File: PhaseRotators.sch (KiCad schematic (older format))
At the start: 10 parts, among them U1 74LVC1G74, U2 74LVC74APW, U3 74LVC74APW, U4 74LVC1G74

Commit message: first edit
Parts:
- removed U1, U4: 74LVC1G74, Housings_SSOP:TSSOP-8_3x3mm_Pitch0.65mm, symbol 74LVC1G74
- removed U3: 74LVC74APW, Housings_SSOP:TSSOP-14_4.4x5mm_Pitch0.65mm, symbol 74LS74
- added R8: 1k, Resistors_SMD:R_0603_HandSoldering, symbol R_Small
- C1, C2: footprint UI:C_1206_0603 -> Capacitors_SMD:C_0603_HandSoldering
- C3: footprint Capacitors_THT:CP_Radial_D5.0mm_P2.00mm -> Capacitors_Tantalum_SMD:CP_Tantalum_Case-A_EIA-3216-18_Wave
- L1: footprint Resistors_THT:R_Axial_DIN0207_L6.3mm_D2.5mm_P10.16mm_Horizontal -> Choke_Axial_ThroughHole:Choke_Horizontal_RM10mm
- R1, R2: footprint UI:R_1206_0603 -> Resistors_SMD:R_0603_HandSoldering
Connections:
- net RX0 is gone; now on an unnamed net: U2.11 (Cp)
- net RX180 is gone; now on an unnamed net: U2.3 (Cp)
- net CLK: now also R2.1
- net GND: now also R8.2
- net at U2.6 (~Q): now also U2.12 (D)
- net P0: now reaches U2.8 (~Q)
- net P0: no longer U2.12 (D)
- net at C1.1, R1.2: now also R8.1; no longer R2.1
- net RX_P0 renamed P90
- net RX_P90: no longer names the net of U2.2 (D), U2.9 (Q)
- net Voltage2 renamed Voltage1
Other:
- moved on the sheet: C1, C2, C3, L1, R1, U2A, U2B

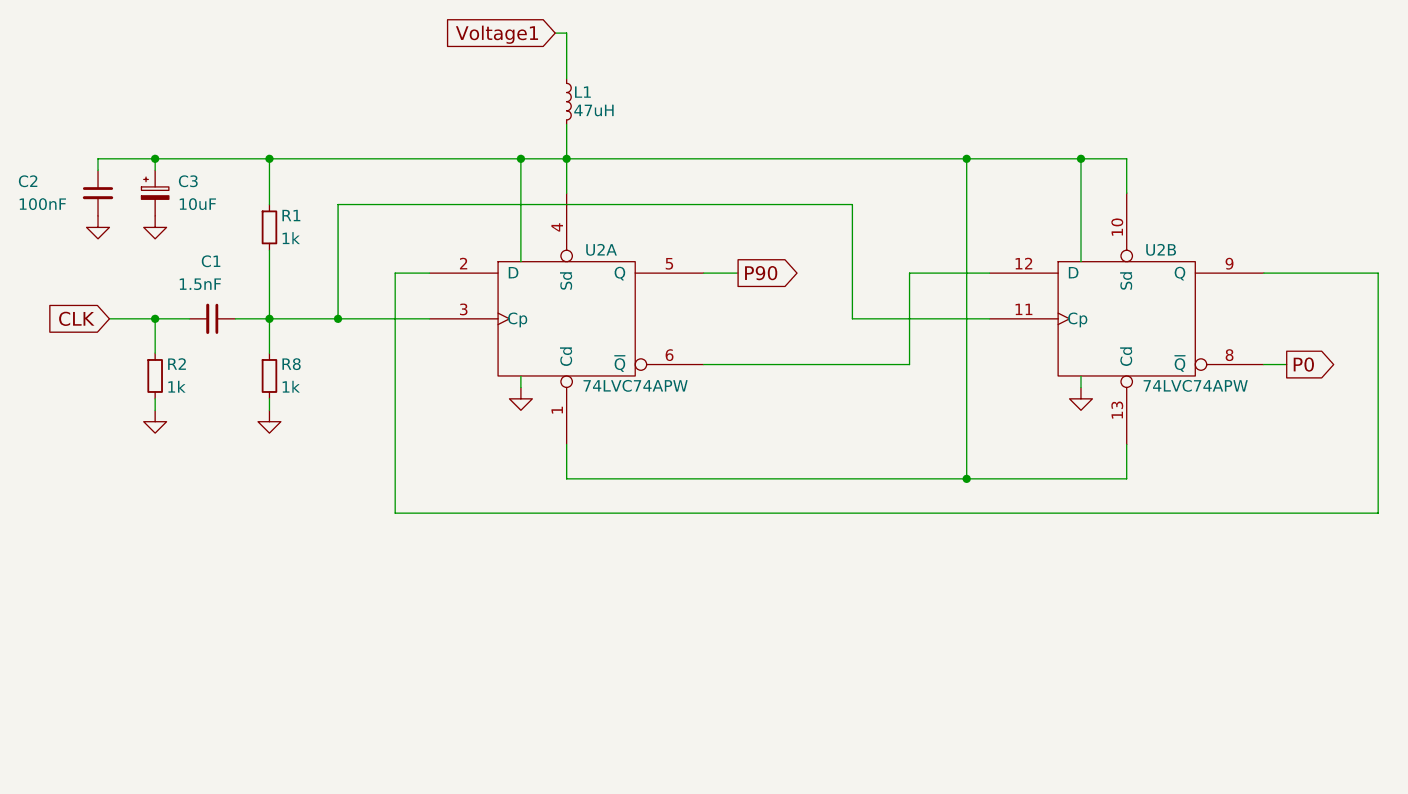
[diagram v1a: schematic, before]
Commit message: rotators 2 74lvc1G74
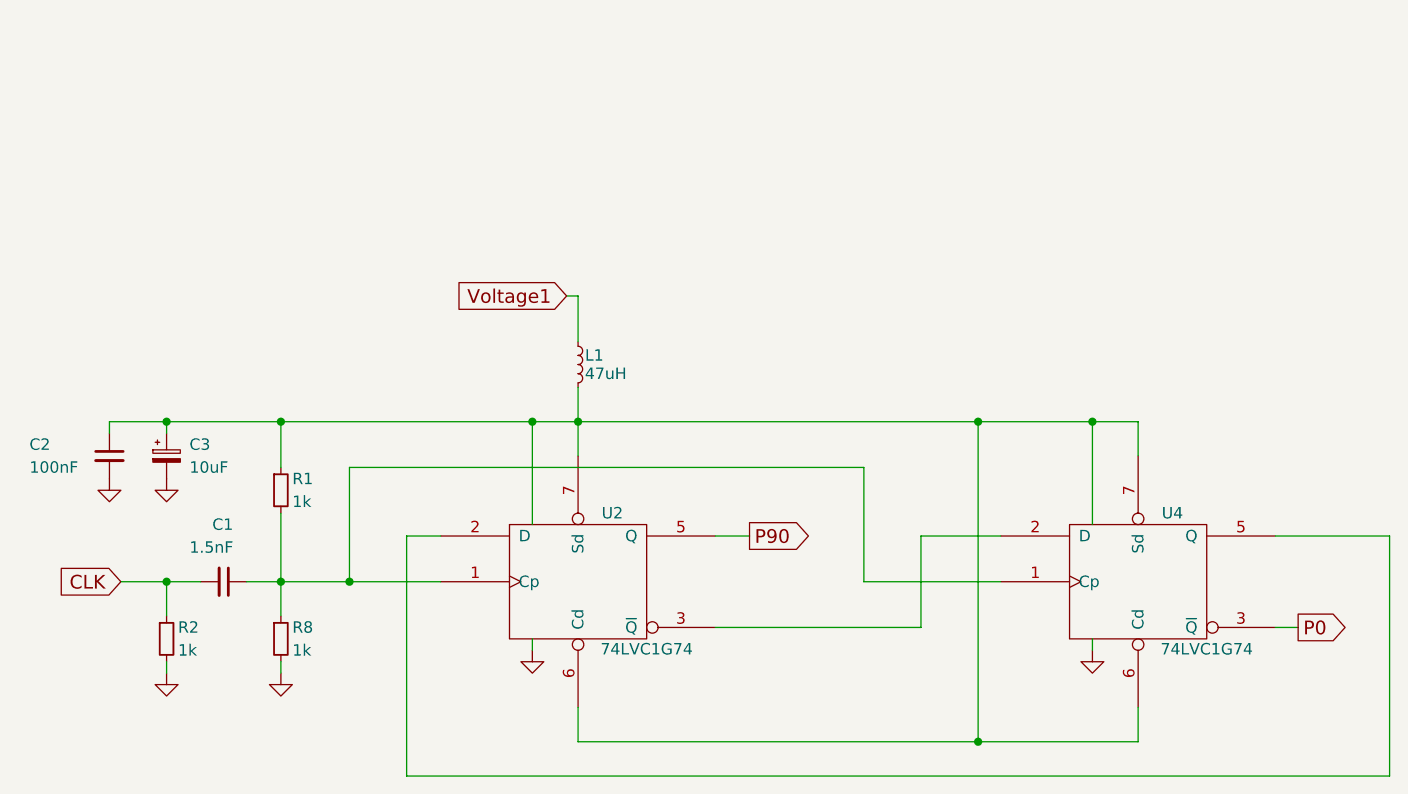
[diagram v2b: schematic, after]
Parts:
- removed U2: 74LVC74APW, Housings_SSOP:TSSOP-14_4.4x5mm_Pitch0.65mm, symbol 74LS74
- added U2, U4: 74LVC1G74, Housings_SSOP:TSSOP-8_4.4x3mm_Pitch0.65mm, symbol 74LVC1G74
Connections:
- net GND: now also U2.4 (GND), U4.4 (GND)
- net P0: now also U4.3 (~Q)
- net P90: now also U2.5 (Q)
- net VCC: now also U2.6 (Cd), U2.7 (Sd), U2.8 (VCC), U4.6 (Cd), U4.7 (Sd), U4.8 (VCC)
- net at C1.1, R1.2, R8.1: now also U2.1 (Cp), U4.1 (Cp)
- new net: U2.2 (D), U4.5 (Q)
- new net: U2.3 (~Q), U4.2 (D)
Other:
- moved on the sheet: C1, C2, C3, L1, R1, R2, R8

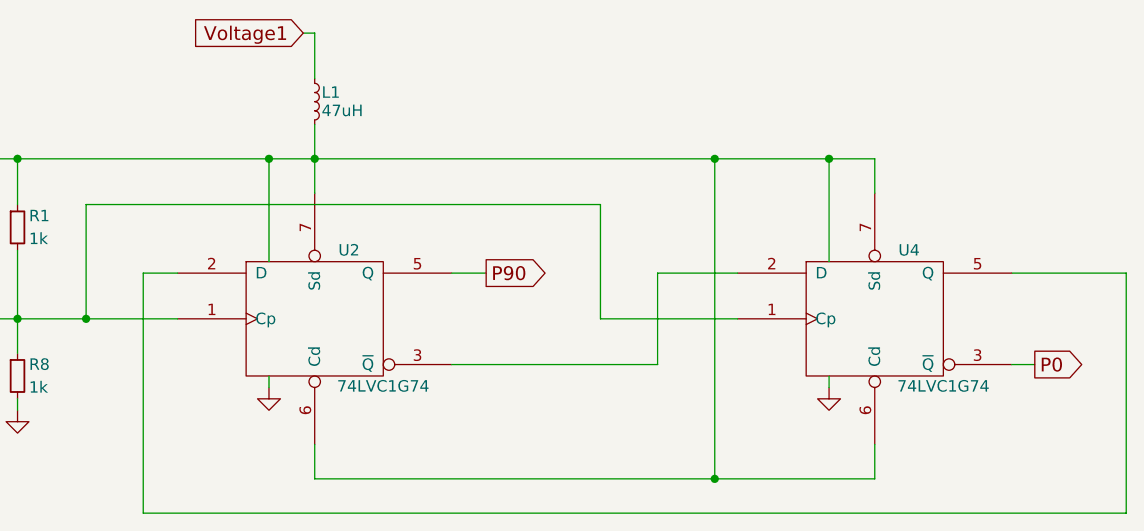
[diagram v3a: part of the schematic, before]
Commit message: need some GND vias
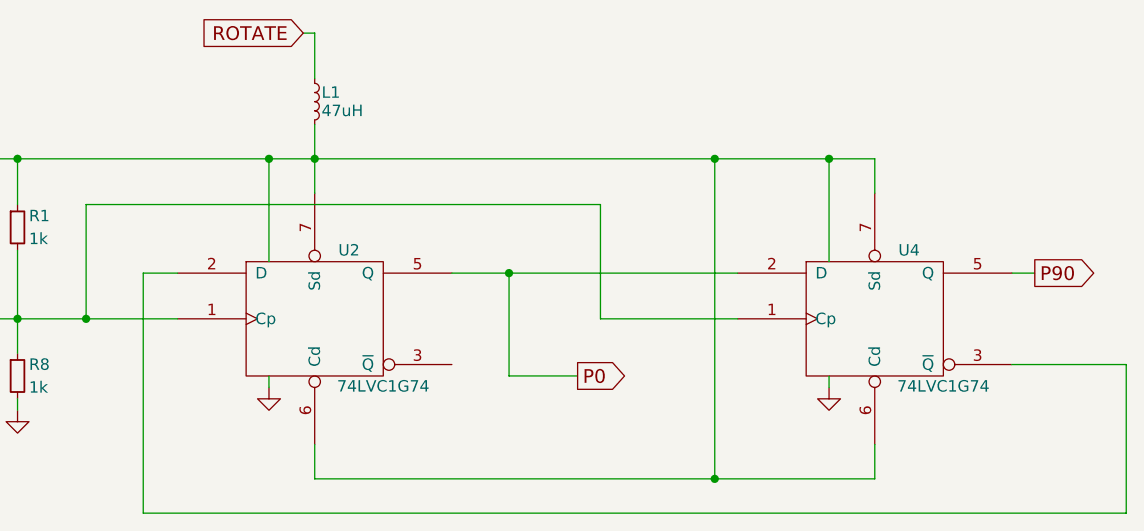
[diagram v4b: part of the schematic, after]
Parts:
- C1, C2: footprint Capacitors_SMD:C_0603_HandSoldering -> UI:C_1206_0603
- C3: footprint Capacitors_Tantalum_SMD:CP_Tantalum_Case-A_EIA-3216-18_Wave -> Capacitors_THT:CP_Radial_D5.0mm_P2.00mm
- R1, R2, R8: footprint Resistors_SMD:R_0603_HandSoldering -> UI:R_1206_0603
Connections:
- net P0: now also U2.5 (Q), U4.2 (D); no longer U4.3 (~Q)
- net P90: now also U4.5 (Q); no longer U2.5 (Q)
- net at U2.2 (D): now also U4.3 (~Q); no longer U4.5 (Q)
- net at U2.3 (~Q): no longer U4.2 (D)
- net Voltage1 renamed ROTATE
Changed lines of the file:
@@
 $Descr A4 11693 8268
 encoding utf-8
-Sheet 5 8
+Sheet 5 7
 Title ""
 Date ""
@@
 	4250 3250 4100 3250
 $Comp
-L GND #PWR019
+L GND #PWR040
 U 1 1 5EACACD6
 P 7100 3750
-F 0 "#PWR019" H 7100 3500 50  0001 C CNN
+F 0 "#PWR040" H 7100 3500 50  0001 C CNN
 F 1 "GND" H 7100 3600 50  0001 C CNN
 F 2 "" H 7100 3750 50  0001 C CNN
@@
 	7100 3750 7100 3700
 $Comp
-L GND #PWR020
+L GND #PWR041
 U 1 1 5EACAD11
 P 4650 3750
-F 0 "#PWR020" H 4650 3500 50  0001 C CNN
+F 0 "#PWR041" H 4650 3500 50  0001 C CNN
 F 1 "GND" H 4650 3600 50  0001 C CNN
 F 2 "" H 4650 3750 50  0001 C CNN
@@
 	4650 3750 4650 3700
 Wire Wire Line
-	6700 3250 6350 3250
+	5450 3250 6700 3250
 Wire Wire Line
 	3400 3450 4250 3450
@@
 Wire Wire Line
 	4100 4300 8400 4300
-Wire Wire Line
-	8400 4300 8400 3250
 $Comp
 L R_Small R1
@@
 F 0 "R1" H 3600 3100 50  0000 L CNN
 F 1 "1k" H 3600 3000 50  0000 L CNN
-F 2 "Resistors_SMD:R_0603_HandSoldering" H 3550 3050 50  0001 C CNN
+F 2 "UI:R_1206_0603" H 3550 3050 50  0001 C CNN
 F 3 "" H 3550 3050 50  0001 C CNN
 	1    3550 3050
@@
 F 0 "C1" V 3050 3400 50  0000 L CNN
 F 1 "1.5nF" V 3150 3300 50  0000 L CNN
-F 2 "Capacitors_SMD:C_0603_HandSoldering" H 3300 3450 50  0001 C CNN
+F 2 "UI:C_1206_0603" H 3300 3450 50  0001 C CNN
 F 3 "" H 3300 3450 50  0001 C CNN
 	1    3300 3450
@@
 F 0 "C3" H 3150 2950 50  0000 L CNN
 F 1 "10uF" H 3150 2850 50  0000 L CNN
-F 2 "Capacitors_Tantalum_SMD:CP_Tantalum_Case-A_EIA-3216-18_Wave" H 3050 2900 50  0001 C CNN
+F 2 "Capacitors_THT:CP_Radial_D5.0mm_P2.00mm" H 3050 2900 50  0001 C CNN
 F 3 "" H 3050 2900 50  0001 C CNN
 	1    3050 2900
@@
 Connection ~ 4650 2750
 $Comp
-L GND #PWR021
+L GND #PWR042
 U 1 1 5EAC7395
 P 3050 3000
-F 0 "#PWR021" H 3050 2750 50  0001 C CNN
+F 0 "#PWR042" H 3050 2750 50  0001 C CNN
 F 1 "GND" H 3050 2850 50  0001 C CNN
 F 2 "" H 3050 3000 50  0001 C CNN
@@
 F 0 "C2" H 2450 2950 50  0000 L CNN
 F 1 "100nF" H 2450 2850 50  0000 L CNN
-F 2 "Capacitors_SMD:C_0603_HandSoldering" H 2800 2900 50  0001 C CNN
+F 2 "UI:C_1206_0603" H 2800 2900 50  0001 C CNN
 F 3 "" H 2800 2900 50  0001 C CNN
 	1    2800 2900
@@
 $EndComp
 $Comp
-L GND #PWR022
+L GND #PWR043
 U 1 1 5EAC76D0
 P 2800 3000
-F 0 "#PWR022" H 2800 2750 50  0001 C CNN
+F 0 "#PWR043" H 2800 2750 50  0001 C CNN
 F 1 "GND" H 2800 2850 50  0001 C CNN
 F 2 "" H 2800 3000 50  0001 C CNN
@@
 	1    0    0    -1
 $EndComp
-Text GLabel 5600 3250 2    60   Output ~ 0
+Text GLabel 6000 3700 2    60   Output ~ 0
+P0
+Text GLabel 8000 3250 2    60   Output ~ 0
 P90
-Text GLabel 8000 3650 2    60   Output ~ 0
-P0
 Text GLabel 4800 2200 0    60   Input ~ 0
-Voltage1
+ROTATE
 Wire Wire Line
 	4800 2200 4850 2200
@@
 	6100 2950 3850 2950
 Connection ~ 3850 3450
-Wire Wire Line
-	6350 3250 6350 3650
-Wire Wire Line
-	6350 3650 5450 3650
-Wire Wire Line
-	8400 3250 7900 3250
-Wire Wire Line
-	5450 3250 5600 3250
-Wire Wire Line
-	7900 3650 8000 3650
 Wire Wire Line
 	3550 3150 3550 3600
@@
 F 0 "R8" H 3600 3750 50  0000 L CNN
 F 1 "1k" H 3600 3650 50  0000 L CNN
-F 2 "Resistors_SMD:R_0603_HandSoldering" H 3550 3700 50  0001 C CNN
+F 2 "UI:R_1206_0603" H 3550 3700 50  0001 C CNN
 F 3 "" H 3550 3700 50  0001 C CNN
 	1    3550 3700
@@
 	3850 2950 3850 3450
 $Comp
-L GND #PWR023
+L GND #PWR044
 U 1 1 5EB0156A
 P 3550 3850
-F 0 "#PWR023" H 3550 3600 50  0001 C CNN
+F 0 "#PWR044" H 3550 3600 50  0001 C CNN
 F 1 "GND" H 3550 3700 50  0001 C CNN
 F 2 "" H 3550 3850 50  0001 C CNN
@@
 F 0 "R2" H 3100 3750 50  0000 L CNN
 F 1 "1k" H 3100 3650 50  0000 L CNN
-F 2 "Resistors_SMD:R_0603_HandSoldering" H 3050 3700 50  0001 C CNN
+F 2 "UI:R_1206_0603" H 3050 3700 50  0001 C CNN
 F 3 "" H 3050 3700 50  0001 C CNN
 	1    3050 3700
@@
 $EndComp
 $Comp
-L GND #PWR024
+L GND #PWR045
 U 1 1 5EB016D4
 P 3050 3850
-F 0 "#PWR024" H 3050 3600 50  0001 C CNN
+F 0 "#PWR045" H 3050 3600 50  0001 C CNN
 F 1 "GND" H 3050 3700 50  0001 C CNN
 F 2 "" H 3050 3850 50  0001 C CNN
@@
 	1    0    0    -1
 $EndComp
+Wire Wire Line
+	8400 4300 8400 3650
+Wire Wire Line
+	5700 3250 5700 3700
+Connection ~ 5700 3250
+Wire Wire Line
+	7900 3250 8000 3250
+Wire Wire Line
+	8400 3650 7900 3650
+Wire Wire Line
+	5700 3700 6000 3700
 $EndSCHEMATC

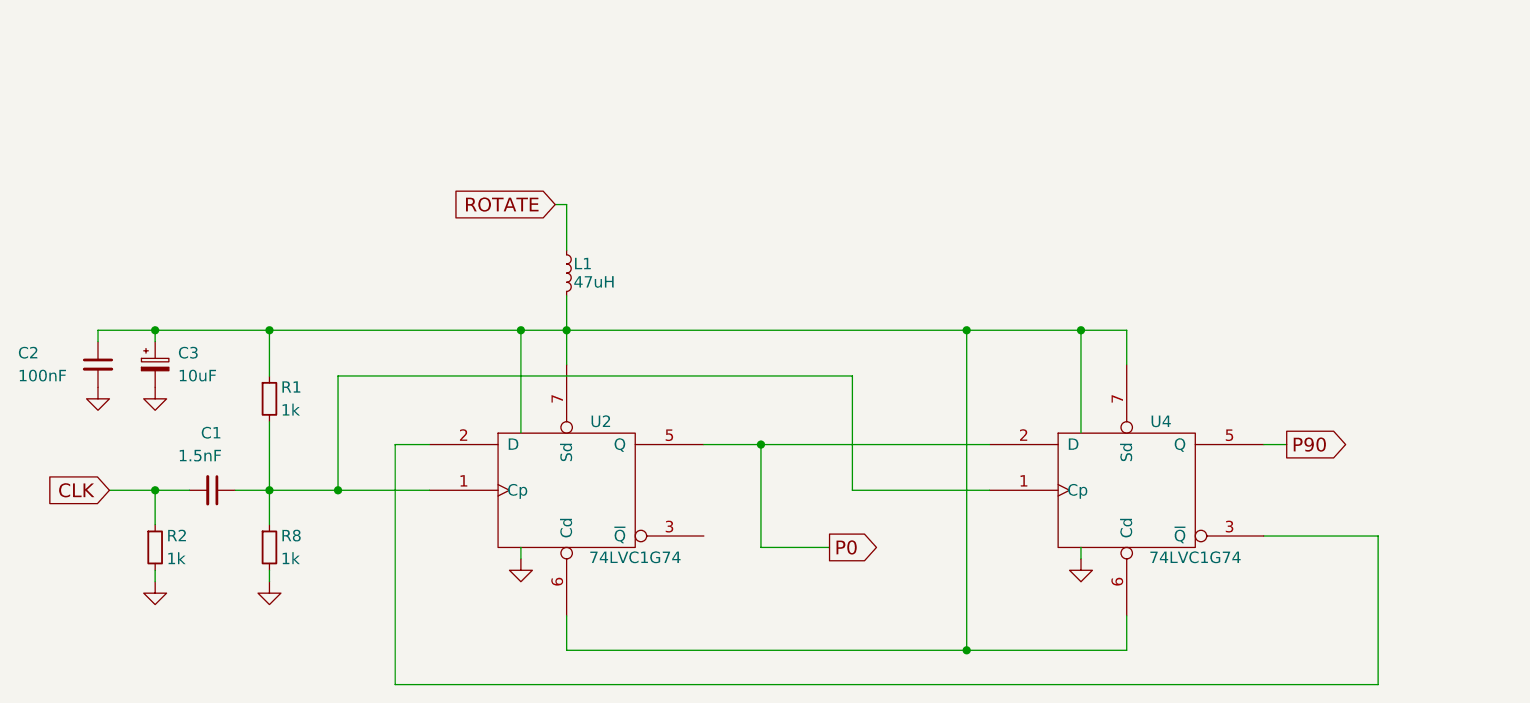
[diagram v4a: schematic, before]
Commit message: Phase shift with 74LCX574 TSSOP-20
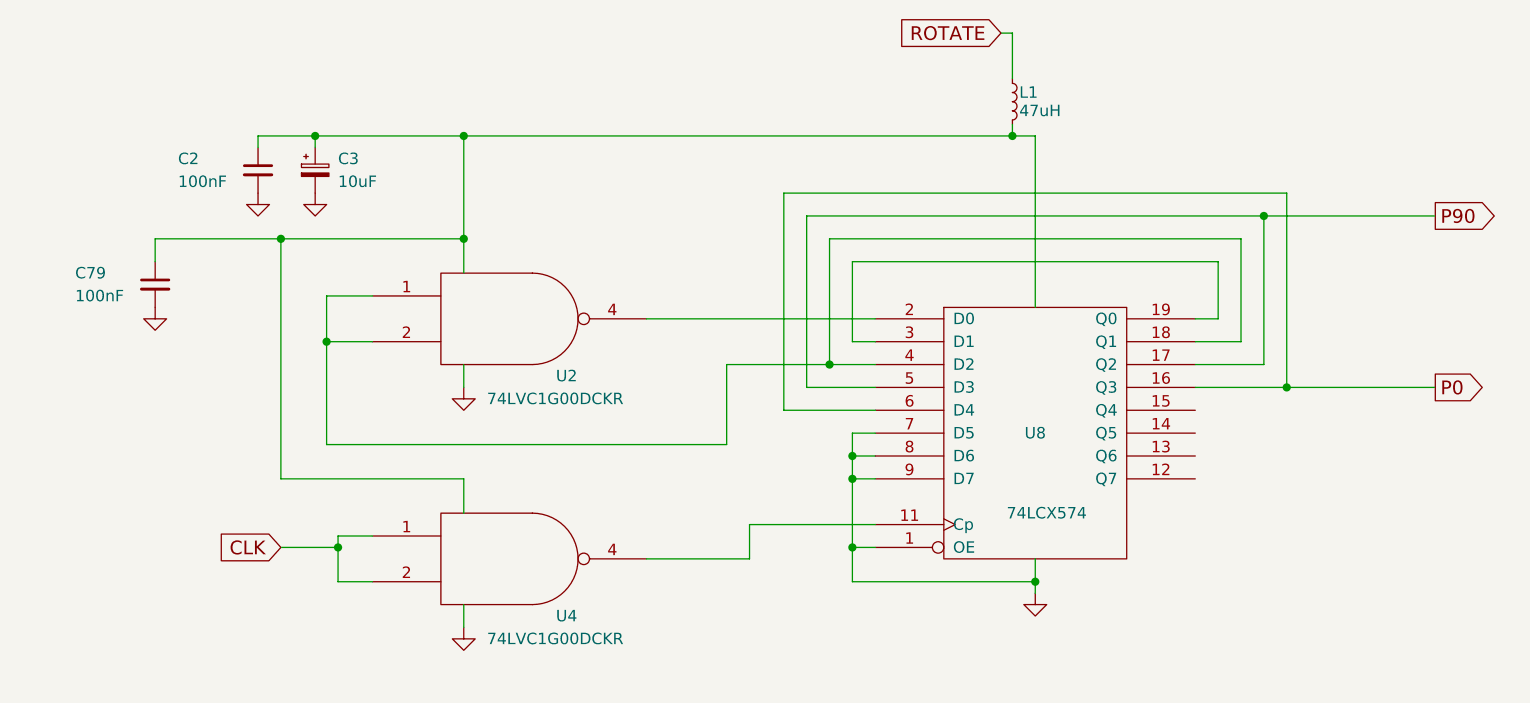
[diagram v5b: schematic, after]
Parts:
- removed C1: 1.5nF, UI:C_1206_0603, symbol C_Small
- removed R1, R2, R8: 1k, UI:R_1206_0603, symbol R_Small
- removed U2, U4: 74LVC1G74, Housings_SSOP:TSSOP-8_4.4x3mm_Pitch0.65mm, symbol 74LVC1G74
- added C79: 100nF, UI:C_1206_0603, symbol C_Small
- added U2, U4: 74LVC1G00DCKR, TO_SOT_Packages_SMD:SOT-353_SC-70-5, symbol 74LVC1G00DCKR
- added U8: 74LCX574, Housings_SSOP:TSSOP-20_4.4x6.5mm_Pitch0.65mm, symbol 74LS574
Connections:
- net CLK: now also U4.1, U4.2
- net GND: now also C79.2, U2.3 (GND), U4.3 (GND), U8.1 (OE), U8.10 (GND), U8.7 (D5), U8.8 (D6), U8.9 (D7)
- net P0: now also U8.16 (Q3), U8.6 (D4)
- net P90: now also U8.17 (Q2), U8.5 (D3)
- net VCC: now also C79.1, U2.5 (VCC), U4.5 (VCC), U8.20 (VCC)
- new net: U4.4, U8.11 (Cp)
- new net: U2.1, U2.2, U8.18 (Q1), U8.4 (D2)
- new net: U8.19 (Q0), U8.3 (D1)
- new net: U2.4, U8.2 (D0)
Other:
- moved on the sheet: C2, C3, L1

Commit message: instrumental amplifier in IF
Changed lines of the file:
@@
 LIBS:cmos4000
 LIBS:conn
-LIBS:pcm2900c
 LIBS:Oscillators
 LIBS:74xx
@@
 $EndComp
 $Comp
-L GND #PWR041
+L GND #PWR43
 U 1 1 5EAC7395
 P 3750 2150
-F 0 "#PWR041" H 3750 1900 50  0001 C CNN
+F 0 "#PWR43" H 3750 1900 50  0001 C CNN
 F 1 "GND" H 3750 2000 50  0001 C CNN
 F 2 "" H 3750 2150 50  0001 C CNN
@@
 $EndComp
 $Comp
-L GND #PWR042
+L GND #PWR42
 U 1 1 5EAC76D0
 P 3500 2150
-F 0 "#PWR042" H 3500 1900 50  0001 C CNN
+F 0 "#PWR42" H 3500 1900 50  0001 C CNN
 F 1 "GND" H 3500 2000 50  0001 C CNN
 F 2 "" H 3500 2150 50  0001 C CNN
@@
 	6900 1900 6900 2650
 $Comp
-L GND #PWR043
+L GND #PWR46
 U 1 1 5ED0A7D2
 P 6900 3900
-F 0 "#PWR043" H 6900 3650 50  0001 C CNN
+F 0 "#PWR46" H 6900 3650 50  0001 C CNN
 F 1 "GND" H 6900 3750 50  0001 C CNN
 F 2 "" H 6900 3900 50  0001 C CNN
@@
 	5550 2900 5550 3250
 Wire Wire Line
-	3800 3250 5550 3250
-Wire Wire Line
-	3800 2600 3800 3250
+	5550 3250 3800 3250
+Wire Wire Line
+	3800 3250 3800 2600
 Wire Wire Line
 	3800 2600 4000 2600
@@
 	4400 2900 4400 3000
 $Comp
-L GND #PWR044
+L GND #PWR44
 U 1 1 5ED0ABB8
 P 4400 3000
-F 0 "#PWR044" H 4400 2750 50  0001 C CNN
+F 0 "#PWR44" H 4400 2750 50  0001 C CNN
 F 1 "GND" H 4400 2850 50  0001 C CNN
 F 2 "" H 4400 3000 50  0001 C CNN
@@
 Connection ~ 4400 2350
 $Comp
-L GND #PWR045
+L GND #PWR45
 U 1 1 5ED1F9E3
 P 4400 4050
-F 0 "#PWR045" H 4400 3800 50  0001 C CNN
+F 0 "#PWR45" H 4400 3800 50  0001 C CNN
 F 1 "GND" H 4400 3900 50  0001 C CNN
 F 2 "" H 4400 4050 50  0001 C CNN
@@
 $EndComp
 $Comp
-L GND #PWR046
+L GND #PWR41
 U 1 1 5ED212C0
 P 3050 2650
-F 0 "#PWR046" H 3050 2400 50  0001 C CNN
+F 0 "#PWR41" H 3050 2400 50  0001 C CNN
 F 1 "GND" H 3050 2500 50  0001 C CNN
 F 2 "" H 3050 2650 50  0001 C CNN
